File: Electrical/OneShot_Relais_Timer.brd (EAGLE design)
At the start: 100 x 80 mm, 26 parts, among them IC1 4511D, IC2 ATTINY204SOIC14, K1 Schrack RE030012, T1 BC847, X1 MKDSN1,5/2-5,08, X2 MKDSN1,5/2-5,08

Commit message: First rough placement of components
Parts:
- moved X2 276.7 mm to (17.8, 50.8)
- moved X1 261.3 mm to (5.08, 50.8)
- moved B1 222.7 mm to (16.5, 16.5), flipped to the bottom
- moved TR1 211.9 mm to (16.5, 31.8), turned to 270 degrees
- moved S2 207.2 mm to (61.0, 29.2), turned to 270 degrees
- moved C1 199.9 mm to (29.2, 11.4), flipped to the bottom
- moved IC2 190.9 mm to (38.1, 33.0), flipped to the bottom
- moved DA1 185.6 mm to (6.35, 12.7), flipped to the bottom
- moved R9 175.9 mm to (44.5, 35.6), flipped to the bottom
- moved R10 175.1 mm to (57.1, 5.08), flipped to the bottom
- moved IC1 174.6 mm to (52.1, 24.1), flipped to the bottom
- moved D2 173.3 mm to (50.8, 24.1)
- moved R8 171.6 mm to (48.3, 35.6), flipped to the bottom
- moved DA2 164.3 mm to (10.4, 4.93), flipped to the bottom
- moved R4 157.9 mm to (59.7, 39.4), flipped to the bottom
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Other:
- board size 100 x 80 mm -> 65 x 63 mm

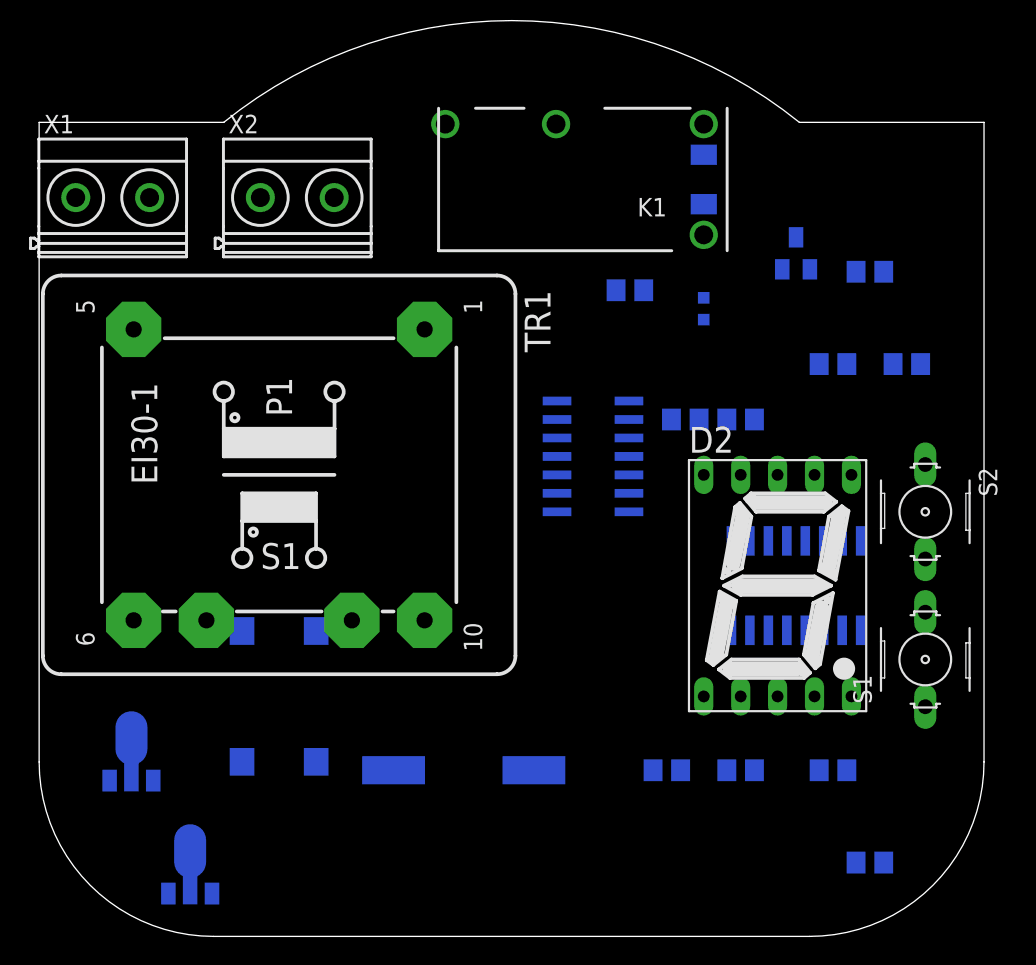
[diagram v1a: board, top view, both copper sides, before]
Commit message: Replaced connectors for AC mains, replaced 12V regulator, added 3D models (trafo, relay, connector X1)
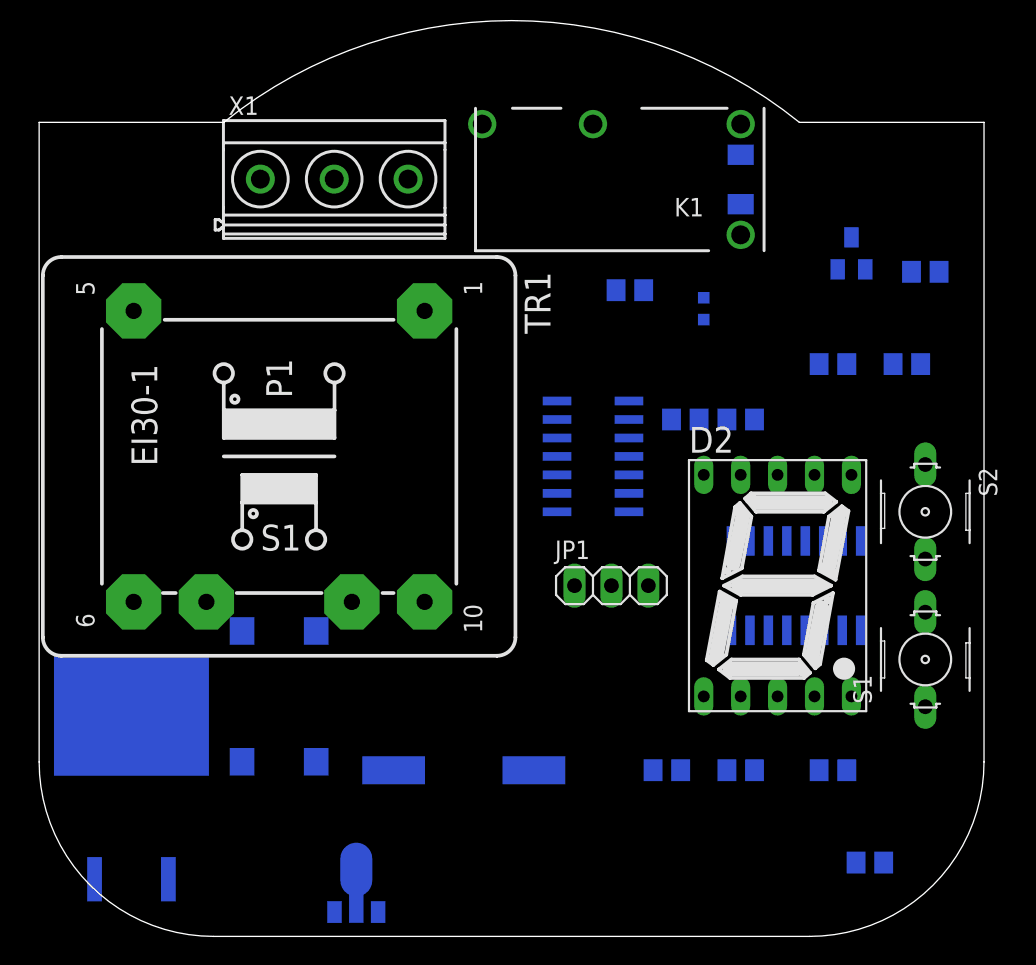
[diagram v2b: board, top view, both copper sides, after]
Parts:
- removed DA1: 78L12SOT89, regulators-linear:SOT89
- removed X2: MKDSN1,5/2-5,08, con-phoenix-508:MKDSN1,5/2-5,08
- added JP1: UPDI, pinhead:1X03
- added U2: MC7812CD2T, _hhn_78xx_79xx_NCV78xx_d2pak_dpak:D2PAK-3
- K1: value Schrack RE030012 -> RE030012; device relay:RE-SCHRACK -> OwnDevices:RE-SCHRACK
- TR1: device trafo:EI30-1 -> OwnDevices:EI30-1
- X1: value MKDSN1,5/2-5,08 -> MKDSN1,5/3-5,08; device con-phoenix-508:MKDSN1,5/2-5,08 -> OwnDevices:MKDSN1,5/3-5,08
- moved X1 17.8 mm to (22.9, 52.1)
- moved DA2 11.5 mm to (21.8, 3.66)
- moved R1 3.81 mm to (61.0, 45.7)
- moved T1 3.81 mm to (55.9, 47.0)
- moved D1 2.54 mm to (48.3, 52.1)
- moved K1 2.54 mm to (39.4, 52.1)
- moved TR1 1.27 mm to (16.5, 33.0)
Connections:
- new net N$26: IC2.10, JP1.1
- net +12V: now also U2.3; no longer DA1.1
- net +5V: now also JP1.2
- net 230V_L_OUT: now also X1.3; no longer X2.2
- net 230V_N: no longer X2.1
- net GND: now also JP1.3, U2.4; no longer DA1.2, DA1.2@1
- net N$21: now also U2.1; no longer DA1.3

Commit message: Replaced 12V and 5V regulators, changed trafo type
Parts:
- removed U2: MC7812CD2T, _hhn_78xx_79xx_NCV78xx_d2pak_dpak:D2PAK-3
- added DA1: 78L12TO220V, regulators-linear:TO220V
- DA2: value 78L05SOT89 -> 78L05SOT223; device regulators-linear:SOT89 -> regulators-linear:SOT223
- moved LED1 18.3 mm to (61.0, 53.3), turned to 180 degrees
- moved R2 15.9 mm to (54.6, 52.1), turned to 180 degrees
- moved DA2 13.9 mm to (8.89, 8.89)
- moved TR1 4.00 mm to (20.5, 33.0)
- moved R8 3.81 mm to (52.1, 35.6)
- moved B1 3.81 mm to (20.3, 16.5)
- moved IC2 3.81 mm to (41.9, 33.0)
- moved R9 3.81 mm to (48.3, 35.6)
- moved C1 3.59 mm to (31.8, 8.89), turned to 270 degrees
- moved JP1 2.54 mm to (41.9, 24.1)
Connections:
- net +12V: now also DA1.3; no longer U2.3
- net GND: now also DA1.2, DA2.4; no longer DA2.2@1, U2.4
- net N$21: now also DA1.1; no longer U2.1

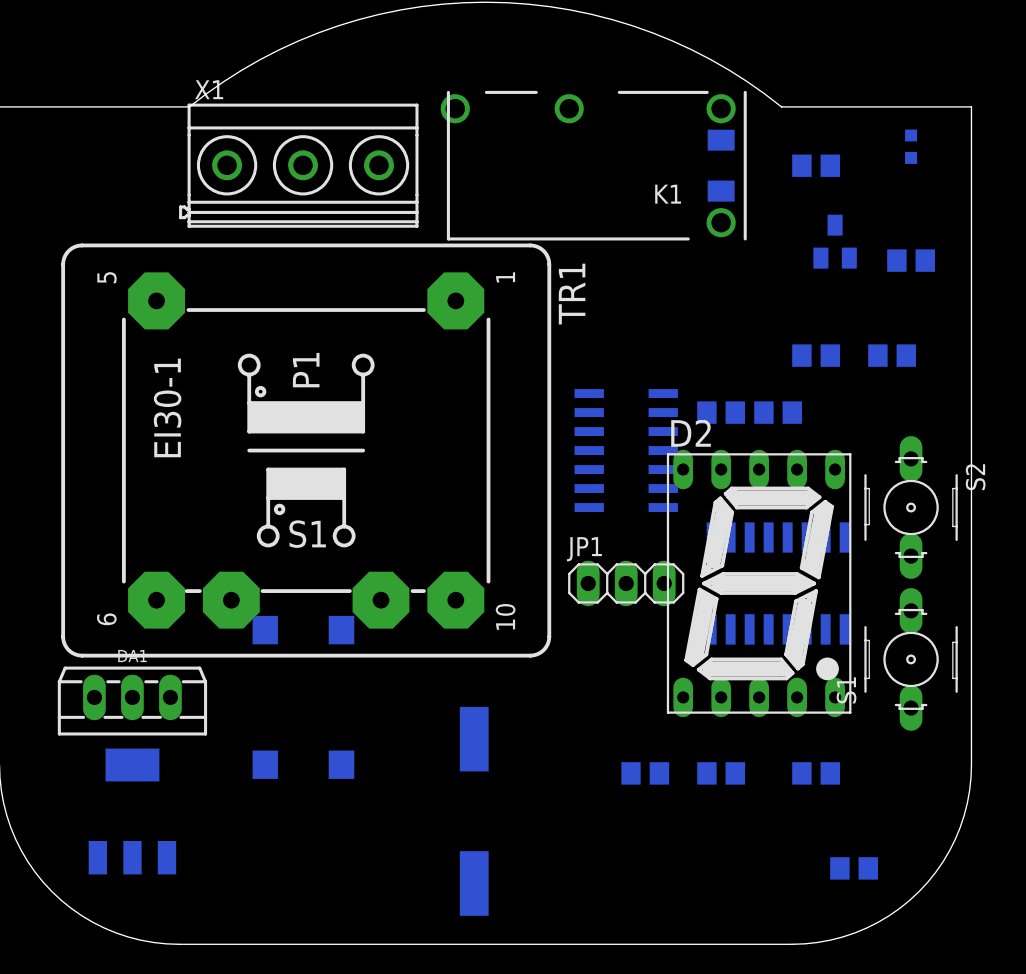
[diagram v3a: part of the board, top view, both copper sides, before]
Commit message: Moved UI components (7 segment, buttons) to separate PCB
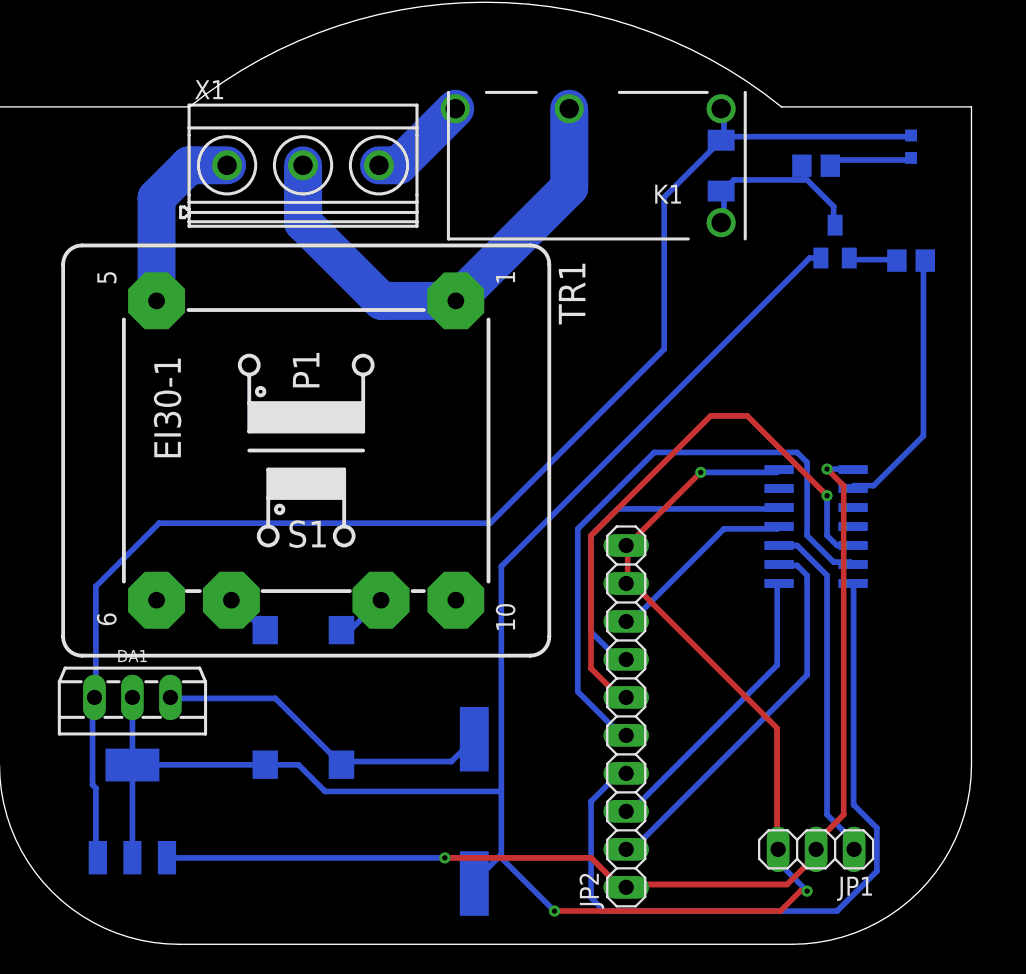
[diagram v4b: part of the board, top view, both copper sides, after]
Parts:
- removed D2: SC56-11EWA, special:7SEG-13
- removed IC1: 4511D, 45xx:SO16
- removed R10, R3, R4, R5, R6, R7, R8, R9: 150, OwnDevices:R0805
- removed S1: SET, OwnDevices:B3F-10XX
- removed S2: START/STOP, OwnDevices:B3F-10XX
- added JP2: (no value), pinhead:1X10
- moved JP1 21.8 mm to (54.6, 6.35), turned to 180 degrees
- moved IC2 13.7 mm to (54.6, 27.9)
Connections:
- removed net N$10: IC1.14, R9.1
- removed net N$11: D2.7, R3.2
- removed net N$12: D2.6, R4.2
- removed net N$13: D2.4, R5.2
- removed net N$14: D2.2, R6.2
- removed net N$15: D2.1, R7.2
- removed net N$16: D2.9, R8.2
- removed net N$17: D2.10, R9.2
- removed net N$18: IC2.12, S2.1
- removed net N$19: D2.5, R10.1
- removed net N$20: IC2.11, S1.1
- removed net N$4: IC1.13, R3.1
- removed net N$5: IC1.12, R4.1
- removed net N$6: IC1.11, R5.1
- removed net N$7: IC1.10, R6.1
- removed net N$8: IC1.9, R7.1
- removed net N$9: IC1.15, R8.1
- new net BTN_SET: IC2.11, JP2.8
- new net BTN_START_STOP: IC2.12, JP2.7
- net +5V: now also JP2.1; no longer IC1.16, IC1.3, IC1.4
- net BCD_7SEG_1: now also JP2.2; no longer IC1.7
- net BCD_7SEG_2: now also JP2.3; no longer IC1.1
- net BCD_7SEG_3: now also JP2.4; no longer IC1.2
- net BCD_7SEG_4: now also JP2.5; no longer IC1.6
- net BCD_7SEG_DOT: now also JP2.6; no longer R10.2
- net GND: now also JP2.10, JP2.9; no longer D2.3, D2.8, IC1.5, IC1.8, S1.2, S2.2
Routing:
- net GND: track 0.00 -> 151.7 mm, vias 0 -> 3
- net +12V: track 0.00 -> 93.6 mm
- net +5V: track 0.00 -> 74.0 mm, vias 0 -> 2
- net BCD_7SEG_3: track 0.00 -> 50.0 mm
- net BCD_7SEG_4: track 0.00 -> 42.0 mm
- net BCD_7SEG_DOT: track 0.00 -> 38.0 mm, vias 0 -> 1
- net 230V_L: track 0.00 -> 32.2 mm
- net BCD_7SEG_1: track 0.00 -> 25.8 mm
- net N$26: track 0.00 -> 23.1 mm
- net N$21: track 0.00 -> 23.0 mm
- net BTN_START_STOP: track 0.00 -> 22.9 mm
- net BCD_7SEG_2: track 0.00 -> 19.7 mm
- net CTRL_RELAY: track 0.00 -> 18.0 mm
- net N$3: track 0.00 -> 13.2 mm
- net BTN_SET: track 0.00 -> 12.9 mm
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
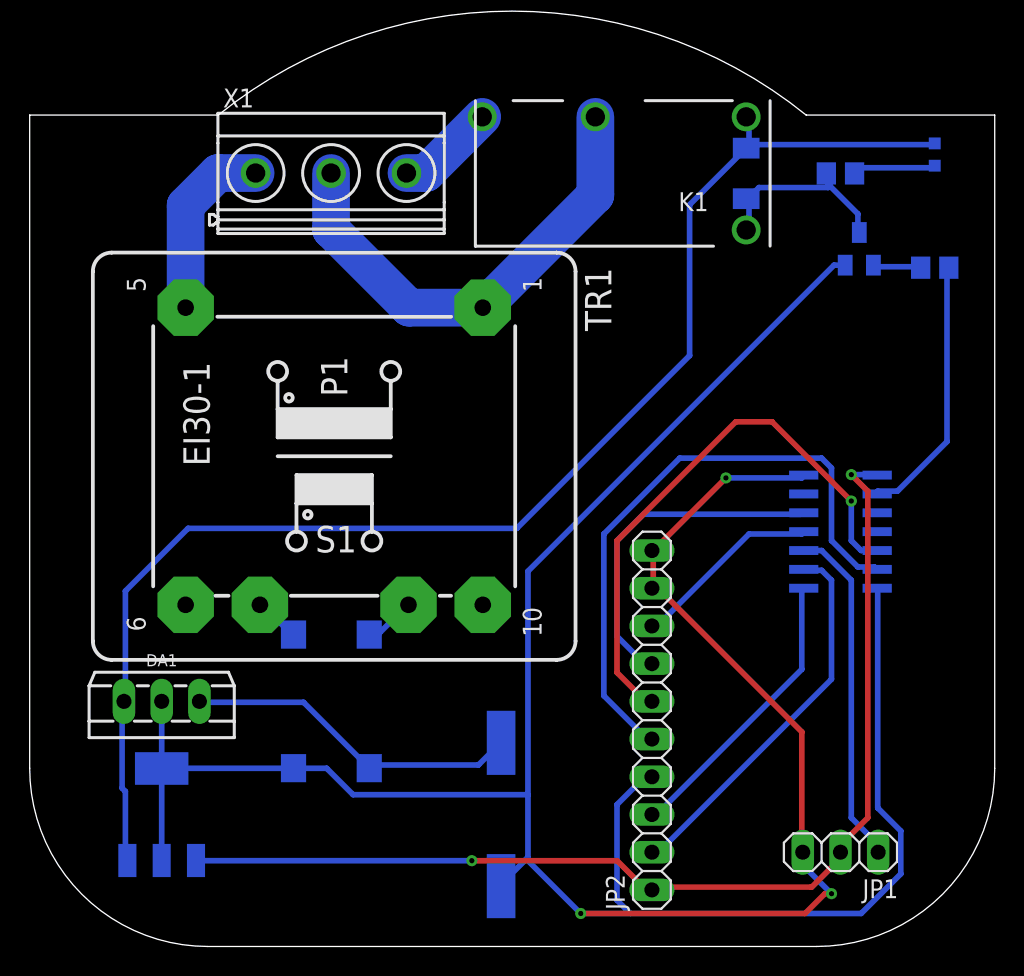
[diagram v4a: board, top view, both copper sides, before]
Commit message: Added mounting holes to PCB, moved relay, small adaptions to UI PCB
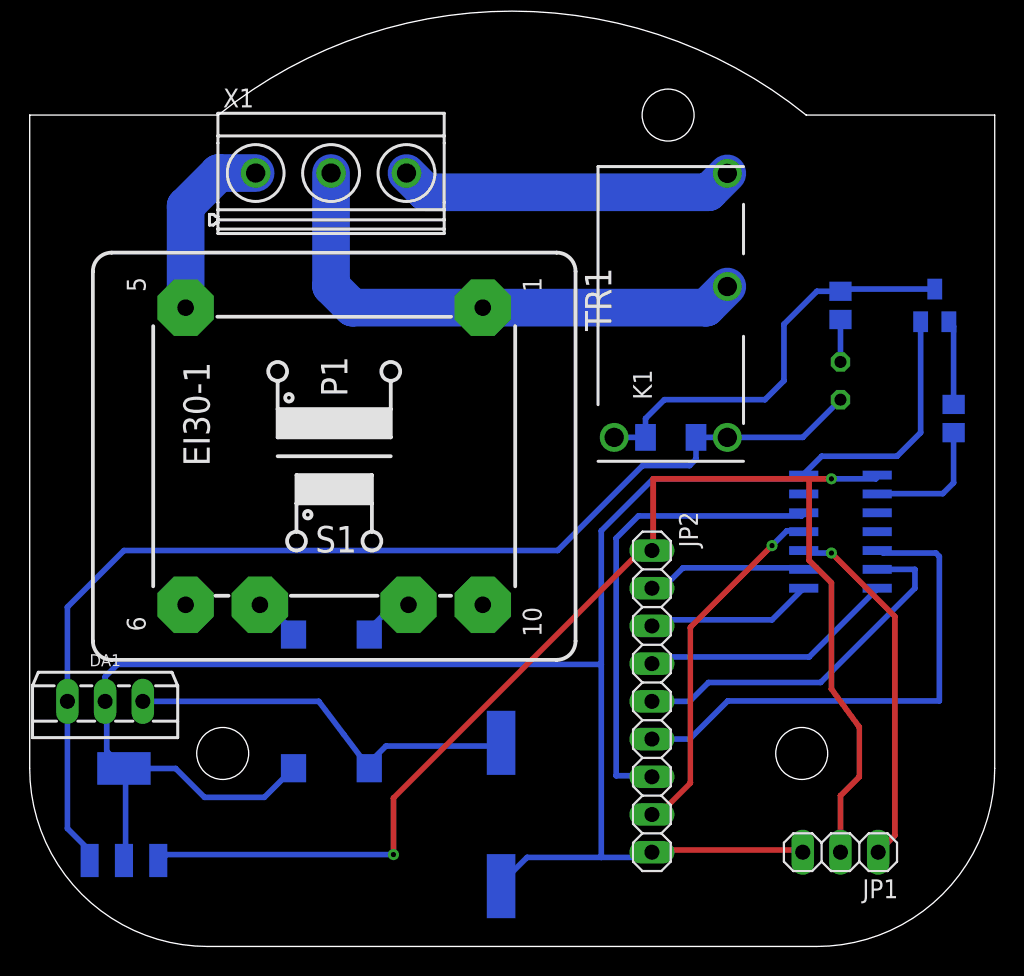
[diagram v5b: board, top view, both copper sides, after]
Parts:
- JP2: device pinhead:1X10 -> pinhead:1X09
- LED1: device OwnDevices:CHIP-LED0603 -> led:LED5MM
- moved D1 18.5 mm to (43.2, 34.3), turned to 0 degrees
- moved LED1 16.5 mm to (54.6, 38.1), turned to 90 degrees
- moved R1 10.2 mm to (62.2, 35.6), turned to 90 degrees
- moved K1 9.67 mm to (43.2, 43.2), turned to 90 degrees
- moved R2 8.89 mm to (54.6, 43.2), turned to 270 degrees
- moved T1 6.35 mm to (61.0, 43.2)
- moved DA1 3.81 mm to (5.08, 14.0)
- moved DA2 2.54 mm to (6.35, 8.89)
- moved JP2 1.27 mm to (41.9, 16.5), turned to 270 degrees
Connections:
- net GND: no longer JP2.10
- net N$2: now also LED1.K; no longer LED1.C
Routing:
- net BCD_7SEG_3: track 50.0 -> 17.5 mm
- net BCD_7SEG_4: track 42.0 -> 24.7 mm
- net +12V: track 93.6 -> 76.4 mm
- net +5V: track 74.0 -> 91.1 mm
- net GND: track 151.7 -> 135.1 mm, vias 3 -> 0
- net 230V_L_OUT: track 6.67 -> 22.7 mm
- net N$3: track 13.2 -> 28.7 mm
- net BCD_7SEG_1: track 25.8 -> 11.0 mm
- net BTN_SET: track 12.9 -> 24.8 mm, vias 0 -> 1
- net CTRL_RELAY: track 18.0 -> 8.83 mm
- net BTN_START_STOP: track 22.9 -> 31.8 mm
- net BCD_7SEG_2: track 19.7 -> 11.4 mm
- net N$21: track 23.0 -> 27.2 mm
- net BCD_7SEG_DOT: track 38.0 -> 34.5 mm, vias 1 -> 0
- net 230V_L: track 32.2 -> 35.5 mm
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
